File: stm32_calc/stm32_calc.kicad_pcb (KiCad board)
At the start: 2 copper layers, 76.2 x 132.2 mm, 75 parts, among them IC1 TM1638, J2 Conn_01x03, J3 C5307759, J4 Conn_02x03_Odd_Even, Q1 p channel mosfet sot 23, SW1 batter_switch, SW2 SS-1290, SW3 Reset, U1 STM32F072CBT6, U2 USBLC6-2SC6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

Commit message: updated pcb
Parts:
- added H1: MountingHole_Pad, MountingHole:MountingHole_2.2mm_M2_DIN965_Pad, F.Cu at (120.8, 92.2)
- added H2: MountingHole_Pad, MountingHole:MountingHole_2.2mm_M2_DIN965_Pad, F.Cu at (120.8, 61.2)
- added H3: MountingHole_Pad, MountingHole:MountingHole_2.2mm_M2_DIN965_Pad, F.Cu at (50.6, 61.2)
- added H4: MountingHole_Pad, MountingHole:MountingHole_2.2mm_M2_DIN965_Pad, F.Cu at (50.6, 92.2)
- added H5: MountingHole_Pad, MountingHole:MountingHole_2.2mm_M2_DIN965_Pad, F.Cu at (85.7, 186.5)
- added H6: MountingHole_Pad, MountingHole:MountingHole_2.2mm_M2_DIN965_Pad, F.Cu at (119.8, 152.4)
- added H7: MountingHole_Pad, MountingHole:MountingHole_2.2mm_M2_DIN965_Pad, F.Cu at (51.6, 152.4)
- moved SW1 4.16 mm to (119.0, 81.9)
- moved J2 0.17 mm to (120.7, 69.3)
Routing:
- net Net-(J2-Pin_3): track 13.0 -> 8.29 mm
- net col0: track 129.8 -> 130.9 mm
- net GND: track 138.3 -> 139.0 mm
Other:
- outline, holes or cut-outs redrawn

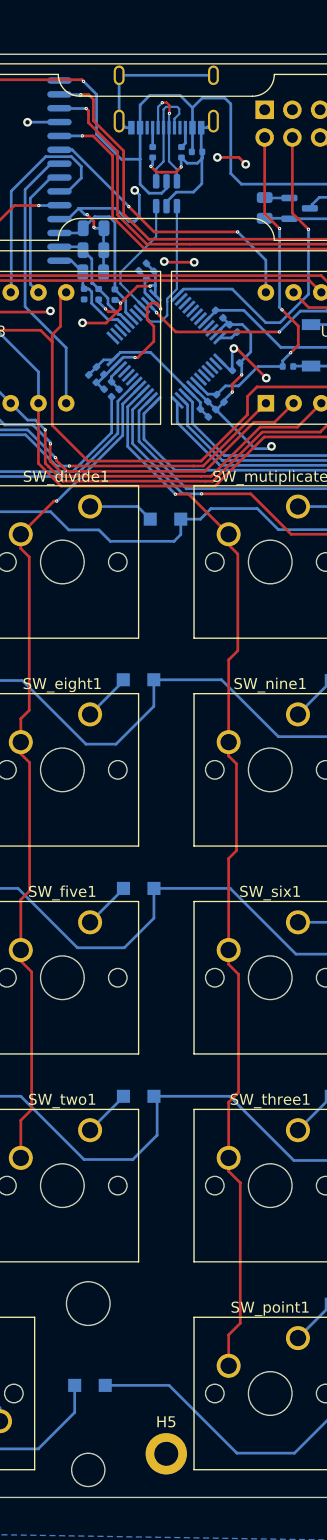
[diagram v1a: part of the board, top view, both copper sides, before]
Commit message: added switch and bottom plate
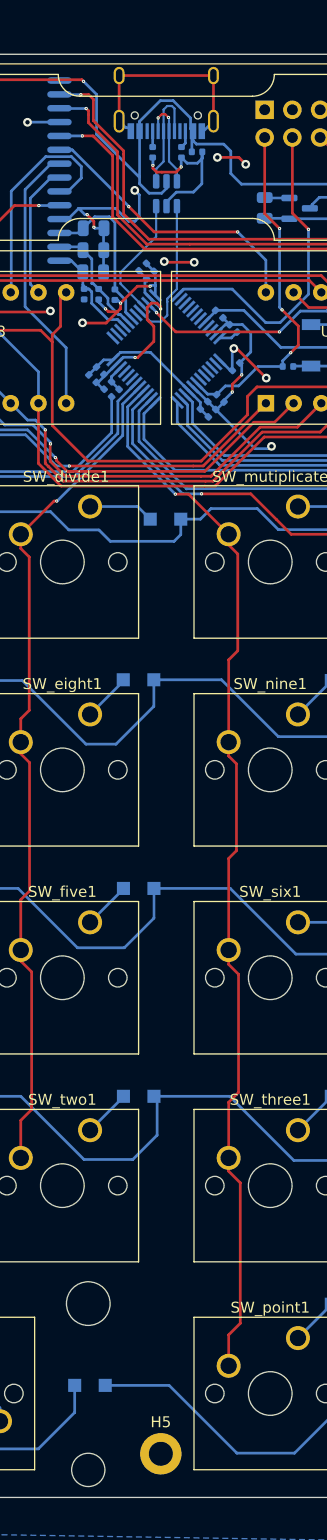
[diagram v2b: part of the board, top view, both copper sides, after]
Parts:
- J3: footprint Connector_USB:USB_C_Receptacle_G-Switch_GT-USB-7010ASV -> Connector_USB:USB_C_Receptacle_HRO_TYPE-C-31-M-12
- moved H5 0.50 mm to (85.2, 186.5)
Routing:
- net vbus: track 128.8 -> 124.0 mm
- net GND: track 139.0 -> 141.0 mm
- net DBUS-: track 10.5 -> 8.60 mm

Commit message: updated pcb
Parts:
- added C11: 100n, Capacitor_SMD:C_0402_1005Metric, B.Cu at (78.4, 61.0)
- moved SW_clear1 26.9 mm to (66.7, 114.3), turned to 180 degrees
- moved D14 26.9 mm to (87.8, 149.4)
- moved SW3 20.2 mm to (97.4, 65.3)
- moved R2 19.7 mm to (92.6, 67.6), turned to -90 degrees
- moved D9 14.8 mm to (83.9, 130.3), turned to 90 degrees
- moved D5 14.7 mm to (65.0, 149.3), turned to 90 degrees
- moved D10 14.7 mm to (83.9, 149.3), turned to 90 degrees
- moved D15 14.6 mm to (103.0, 168.3), turned to 90 degrees
- moved D6 14.6 mm to (64.9, 168.3), turned to 90 degrees
- moved D4 14.6 mm to (64.8, 130.2), turned to 90 degrees
- moved D13 14.6 mm to (102.8, 130.2), turned to 90 degrees
- moved D11 14.6 mm to (83.5, 168.3), turned to 90 degrees
- moved D17 14.2 mm to (106.9, 111.5), turned to 90 degrees
- moved J4 13.1 mm to (107.7, 62.1), turned to 180 degrees
- moved SW_six1 11.4 mm to (92.7, 148.0), turned to 180 degrees
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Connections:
- J3 pad A6: DBUS+ -> D+
- J3 pad A7: DBUS- -> D-
- J3 pad B6: DBUS+ -> D+
- J3 pad B7: DBUS- -> D-
- U2 pad 4: DBUS+ -> D+
- U2 pad 6: DBUS- -> D-
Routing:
- net vbus: track 124.0 -> 69.8 mm, vias 2 -> 3
- net GND: track 141.0 -> 91.8 mm
- net row0: track 81.7 -> 108.9 mm
- net +3V3: track 55.4 -> 33.1 mm, vias 12 -> 6
- net GR2: track 84.4 -> 63.7 mm, vias 1 -> 2
- net GR7: track 70.6 -> 88.1 mm, vias 0 -> 1
- net col0: track 130.9 -> 113.7 mm
- net row3: track 175.0 -> 159.1 mm
- net Net-(D16-A): track 4.37 -> 19.8 mm
- net row4: track 182.5 -> 167.2 mm
- net Net-(D14-A): track 18.7 -> 4.92 mm
- net col2: track 97.4 -> 109.8 mm, vias 1 -> 0
- net row1: track 133.2 -> 121.0 mm
- net row2: track 150.9 -> 139.6 mm
- net D+: track 11.5 -> 22.3 mm
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
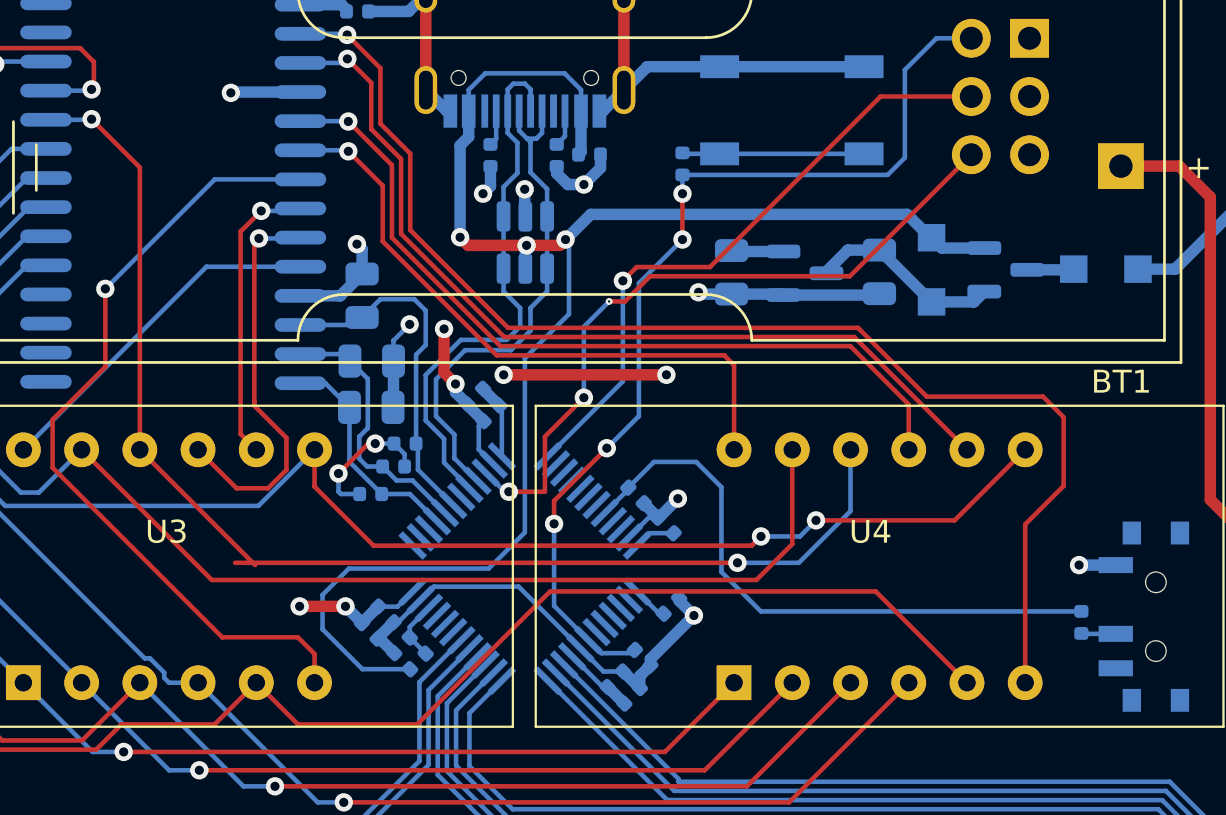
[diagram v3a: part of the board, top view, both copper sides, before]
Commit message: fixed resistor footprints
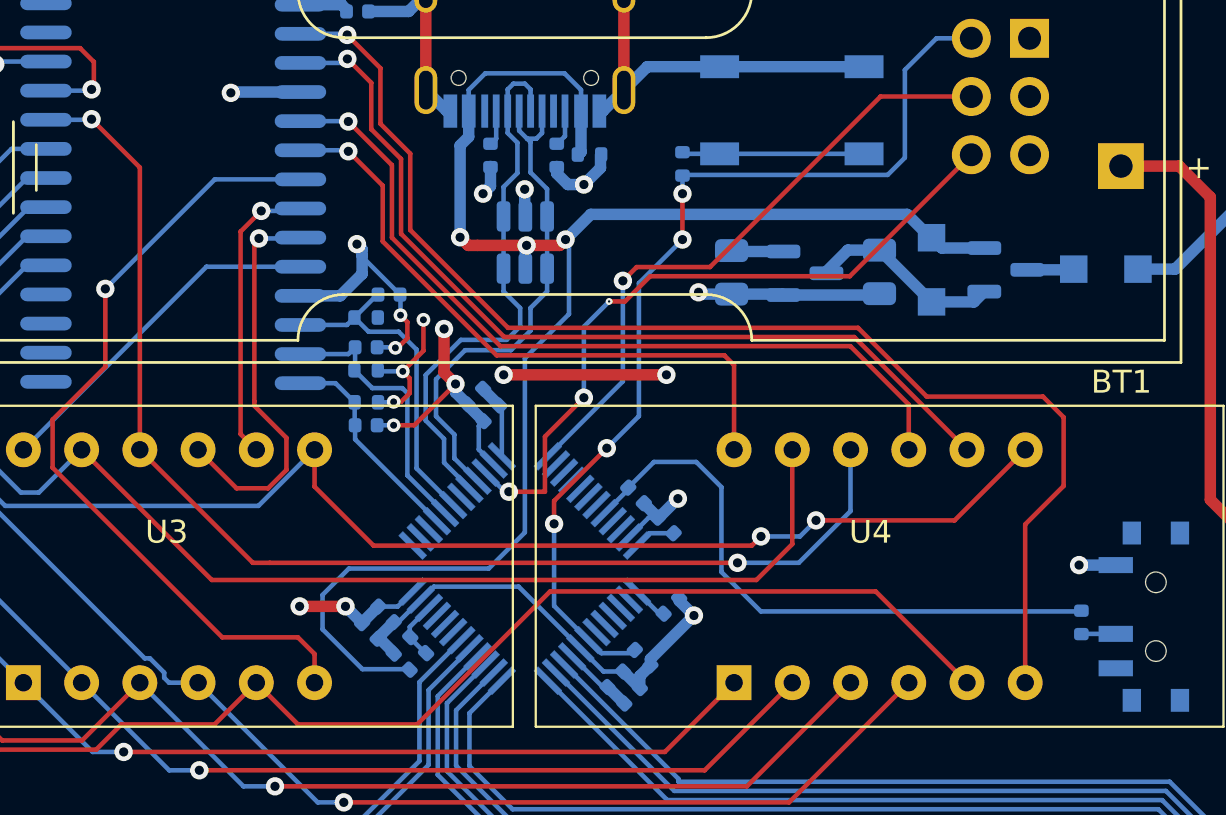
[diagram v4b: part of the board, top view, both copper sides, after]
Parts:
- C15, C16, C17: footprint Capacitor_SMD:C_0805_2012Metric -> Capacitor_SMD:C_0402_1005Metric
- D2: value 1n4001 -> 1n4148
- R1, R10, R11, R12, R13, R2, R5, R6, R7, R8: footprint Capacitor_SMD:C_0402_1005Metric -> Resistor_SMD:R_0402_1005Metric
- moved R7 5.76 mm to (78.8, 74.3), turned to 0 degrees
- moved R6 4.37 mm to (78.8, 76.6)
- moved R5 4.00 mm to (78.8, 78.0), turned to 0 degrees
- moved C17 1.18 mm to (79.8, 73.3), turned to 180 degrees
- moved C15 0.81 mm to (78.8, 79.0)
- moved C16 0.65 mm to (78.8, 75.6)
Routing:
- net GND: track 91.8 -> 97.9 mm, vias 12 -> 14
- net GR6: track 54.9 -> 53.9 mm
- net DIO: track 15.5 -> 14.7 mm
- net +3V3: track 33.1 -> 33.5 mm, vias 6 -> 7

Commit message: updated pcb
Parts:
- moved R12 12.4 mm to (88.9, 79.7), turned to 45 degrees
- moved R11 12.3 mm to (89.6, 80.4), turned to -135 degrees
- moved C19 8.77 mm to (100.0, 63.6)
- moved U5 8.77 mm to (96.8, 63.7)
- moved C20 8.77 mm to (93.6, 63.6)
- moved D2 8.77 mm to (102.3, 63.5)
- moved Q1 8.77 mm to (105.5, 63.5)
- moved D1 8.77 mm to (109.9, 63.5)
- moved J4 6.44 mm to (108.4, 68.5)
- moved SW3 4.55 mm to (96.7, 69.8)
- moved R2 4.55 mm to (91.9, 72.1)
- moved R5 0.98 mm to (78.2, 78.7), turned to -90 degrees
- moved R7 0.91 mm to (78.2, 73.7), turned to 90 degrees
- moved C16 0.74 mm to (79.2, 76.2), turned to 90 degrees
- moved C17 0.74 mm to (79.2, 73.7), turned to -90 degrees
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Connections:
- U1 pad 22: usb_check_mcu -> unconnected-(U1-PB11/TIM2_CH4/I2C2_SDA-Pad22)
- U1 pad 41: unconnected-(U1-SPI1_MOSI/I2S1_SD/TIM3_CH2/PB5-Pad41) -> usb_check_mcu
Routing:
- net +3V3: track 33.5 -> 17.0 mm, vias 7 -> 0
- net GND: track 97.9 -> 84.8 mm
- net vbus: track 69.8 -> 58.9 mm, vias 3 -> 6
- net SWDIO: track 30.8 -> 25.8 mm, vias 3 -> 2
- net NRST: track 42.9 -> 38.0 mm, vias 4 -> 1
- net SWCLK: track 27.5 -> 23.0 mm, vias 1 -> 0
- net Net-(D1-A): track 9.45 -> 11.8 mm
- net DIO: track 14.7 -> 13.2 mm
- net STB: track 9.38 -> 10.0 mm
- net CLK: track 12.2 -> 11.6 mm
